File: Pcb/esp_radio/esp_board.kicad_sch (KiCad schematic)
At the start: 15 parts, among them J2 JTAG_ESP1, SW1 Reset, SW2 Boot, U3 ESP32-WROVER_IE

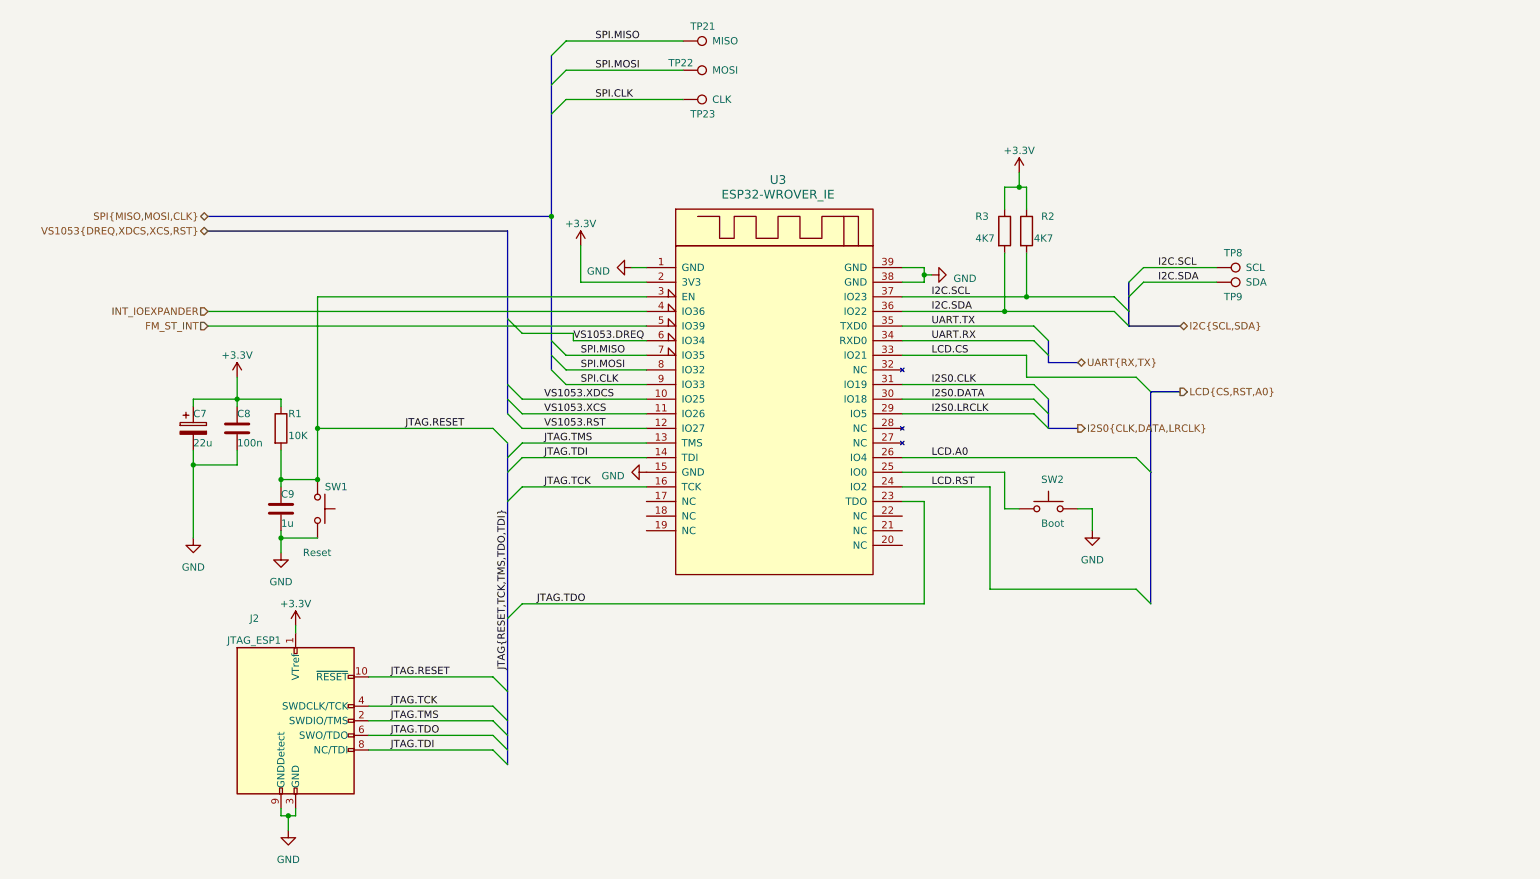
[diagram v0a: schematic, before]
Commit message: Move custom components to kicad_common_library.
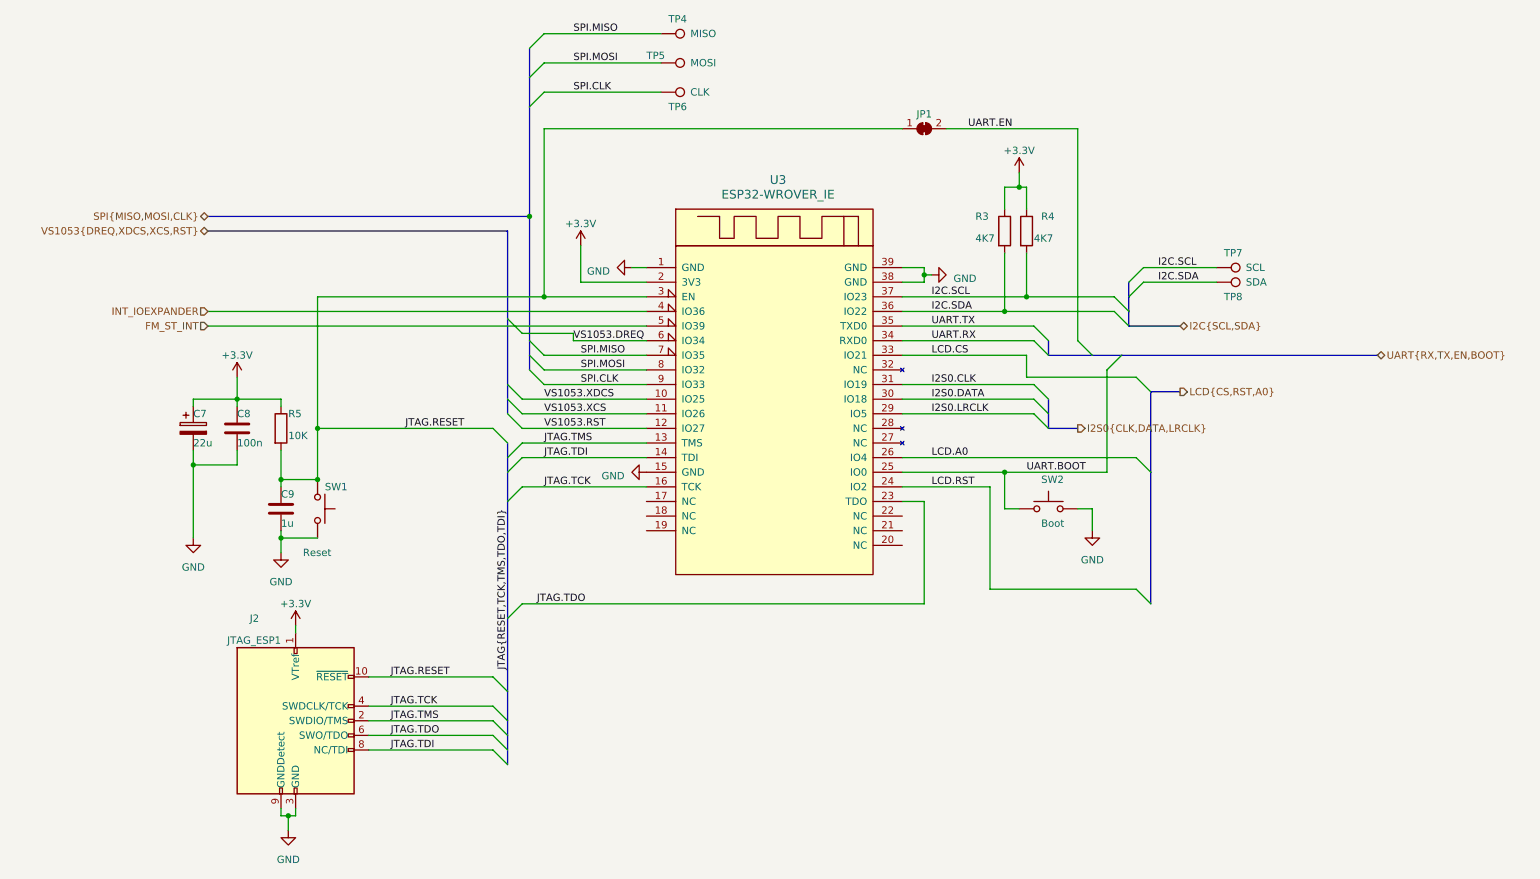
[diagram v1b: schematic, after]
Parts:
- added JP1: SolderJumper_2_Bridged, Jumper:SolderJumper-2_P1.3mm_Bridged_RoundedPad1.0x1.5mm, symbol Jumper:SolderJumper_2_Bridged
- U3: symbol KicadCommon:ESP32-WROVER -> kicad_common_lib:ESP32-WROVER
- renumbered R2 to R4, R1 to R5, TP21 to TP4, TP22 to TP5, TP23 to TP6, TP8 to TP7, TP9 to TP8
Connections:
- net JTAG.RESET: now also JP1.1 (A)
- net UART.BOOT: now reaches SW2.1, U3.25 (IO0)
- new net UART.EN: JP1.2 (B)
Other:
- moved on the sheet: TP4, TP5, TP6

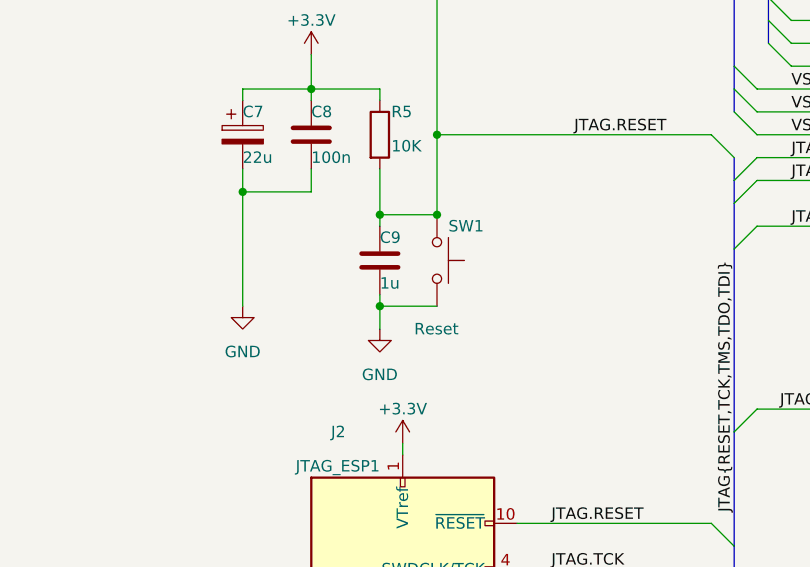
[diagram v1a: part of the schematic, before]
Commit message: Add components layout on PCB
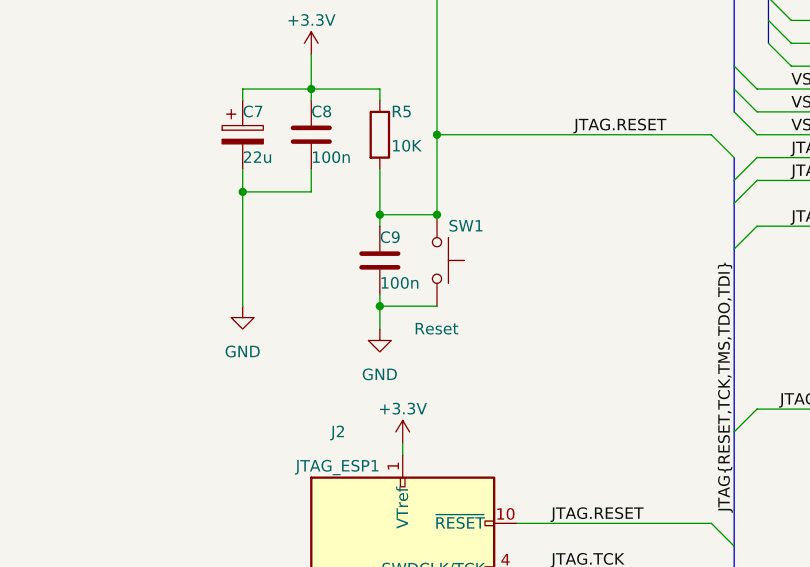
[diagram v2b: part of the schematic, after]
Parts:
- C9: value 1u -> 100n
- R3, R4: footprint Resistor_SMD:R_0805_2012Metric_Pad1.20x1.40mm_HandSolder -> kicad_common_lib:R_0805
- TP4, TP5, TP6, TP7, TP8: footprint (none) -> TestPoint:TestPoint_THTPad_D2.0mm_Drill1.0mm
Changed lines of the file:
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@@
       (effects (font (size 1.27 1.27)) (justify left))
     )
-    (property "Footprint" "" (at 128.27 46.99 0)
+    (property "Footprint" "TestPoint:TestPoint_THTPad_D2.0mm_Drill1.0mm" (at 128.27 46.99 0)
       (effects (font (size 1.27 1.27)) hide)
     )
@@
       (effects (font (size 1.27 1.27)) (justify left))
     )
-    (property "Footprint" "" (at 224.79 80.01 0)
+    (property "Footprint" "TestPoint:TestPoint_THTPad_D2.0mm_Drill1.0mm" (at 224.79 80.01 0)
       (effects (font (size 1.27 1.27)) hide)
     )
@@
       (effects (font (size 1.27 1.27)) (justify left))
     )
-    (property "Footprint" "" (at 224.79 77.47 0)
+    (property "Footprint" "TestPoint:TestPoint_THTPad_D2.0mm_Drill1.0mm" (at 224.79 77.47 0)
       (effects (font (size 1.27 1.27)) hide)
     )
@@
       (effects (font (size 1.27 1.27)) (justify left))
     )
-    (property "Value" "1u" (at 62.23 116.84 0)
+    (property "Value" "100n" (at 62.23 116.84 0)
       (effects (font (size 1.27 1.27)) (justify left))
     )
@@
       (effects (font (size 1.27 1.27)) (justify left))
     )
-    (property "Footprint" "Resistor_SMD:R_0805_2012Metric_Pad1.20x1.40mm_HandSolder" (at 189.992 66.04 90)
+    (property "Footprint" "kicad_common_lib:R_0805" (at 189.992 66.04 90)
       (effects (font (size 1.27 1.27)) hide)
     )
@@
       (effects (font (size 1.27 1.27)) (justify left))
     )
-    (property "Footprint" "" (at 128.27 41.91 0)
+    (property "Footprint" "TestPoint:TestPoint_THTPad_D2.0mm_Drill1.0mm" (at 128.27 41.91 0)
       (effects (font (size 1.27 1.27)) hide)
     )
@@
       (effects (font (size 1.27 1.27)) (justify left))
     )
-    (property "Footprint" "Resistor_SMD:R_0805_2012Metric_Pad1.20x1.40mm_HandSolder" (at 186.182 66.04 90)
+    (property "Footprint" "kicad_common_lib:R_0805" (at 186.182 66.04 90)
       (effects (font (size 1.27 1.27)) hide)
     )
@@
       (effects (font (size 1.27 1.27)) (justify left))
     )
-    (property "Footprint" "" (at 128.27 36.83 0)
-      (effects (font (size 1.27 1.27)) hide)
-    )
+    (property "Footprint" "TestPoint:TestPoint_THTPad_D2.0mm_Drill1.0mm" (at 128.27 36.83 0)
+      (effects (font (size 1.27 1.27)) hide)
+    )

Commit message: Finish board routing
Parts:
- added J11: IR, Connector_PinHeader_1.00mm:PinHeader_1x01_P1.00mm_Vertical, symbol Connector_Generic:Conn_01x01
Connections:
- net JTAG.TDO: now also J11.1 (Pin_1)
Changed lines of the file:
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@@
   (junction (at 46.99 106.68) (diameter 0.9144) (color 0 0 0 0)
   )
+  (junction (at 173.99 130.81) (diameter 0) (color 0 0 0 0)
+  )
   (junction (at 62.23 119.38) (diameter 0.9144) (color 0 0 0 0)
   )
@@
   (wire (pts (xy 77.47 143.51) (xy 99.06 143.51))
     (stroke (width 0) (type solid))
+  )
+  (wire (pts (xy 173.99 130.81) (xy 173.99 139.7))
+    (stroke (width 0) (type default))
   )
   (bus (pts (xy 105.41 39.37) (xy 105.41 44.45))
@@
         )
       )
+    )
+  )
+  (symbol (lib_id "Connector_Generic:Conn_01x01") (at 179.07 139.7 0) (unit 1)
+    (in_bom yes) (on_board yes) (dnp no) (fields_autoplaced)
+    (property "Reference" "J11" (at 181.61 139.065 0)
+      (effects (font (size 1.27 1.27)) (justify left))
+    )
+    (property "Value" "IR" (at 181.61 141.605 0)
+      (effects (font (size 1.27 1.27)) (justify left))
+    )
+    (property "Footprint" "Connector_PinHeader_1.00mm:PinHeader_1x01_P1.00mm_Vertical" (at 179.07 139.7 0)
+      (effects (font (size 1.27 1.27)) hide)
+    )
+    (property "Datasheet" "~" (at 179.07 139.7 0)
+      (effects (font (size 1.27 1.27)) hide)
+    )
+    (pin "1")
+    (instances
+      (project "esp_radio"
+        (path "/c9e2e0d2-0655-4f5e-8e13-71b41b1f7cfe/925b05c5-5253-4c9a-b090-487f8e9d1815"
+          (reference "J11") (unit 1)
+        )
+      )

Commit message: Add chip select emulation for i2c devices
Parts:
- J11: footprint Connector_PinHeader_1.00mm:PinHeader_1x01_P1.00mm_Vertical -> Connector_PinHeader_2.54mm:PinHeader_1x01_P2.54mm_Vertical
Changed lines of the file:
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@@
       (effects (font (size 1.27 1.27)) (justify left))
     )
-    (property "Footprint" "Connector_PinHeader_1.00mm:PinHeader_1x01_P1.00mm_Vertical" (at 179.07 139.7 0)
+    (property "Footprint" "Connector_PinHeader_2.54mm:PinHeader_1x01_P2.54mm_Vertical" (at 179.07 139.7 0)
       (effects (font (size 1.27 1.27)) hide)
     )

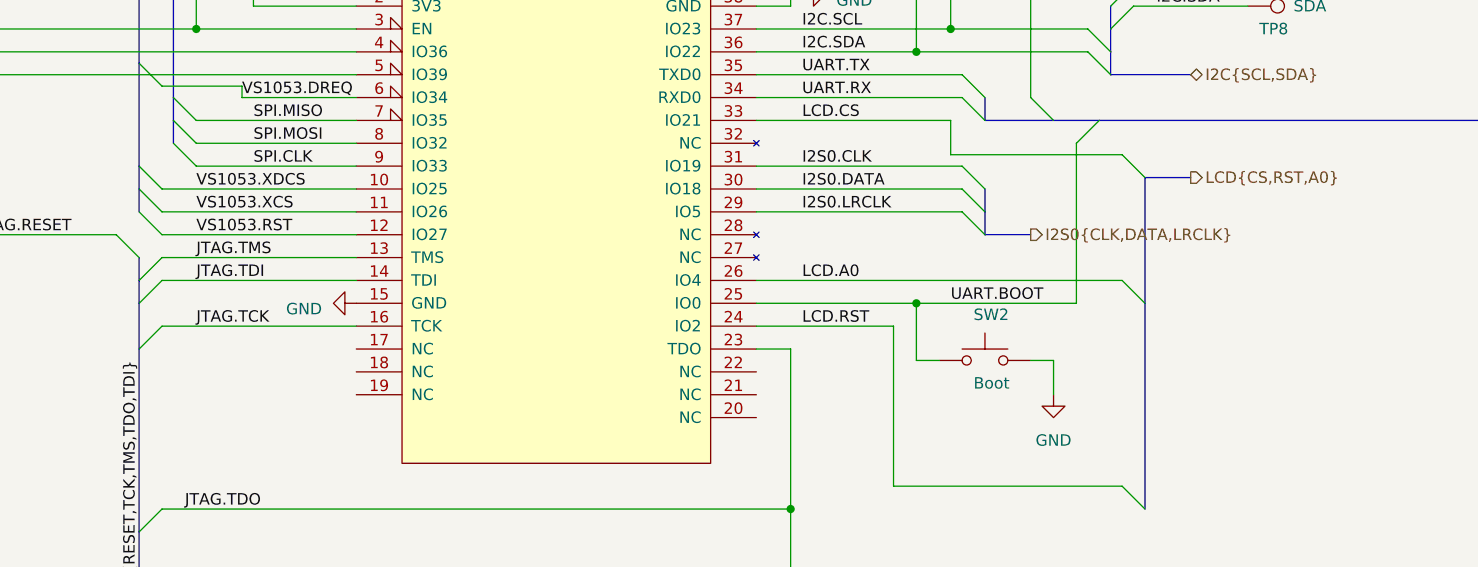
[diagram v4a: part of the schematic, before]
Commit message: Pcb. Fix hw issues.
Add loop to esp32 after i2s switcher
esp32 can convert stream to format compatible to MerusAudio.
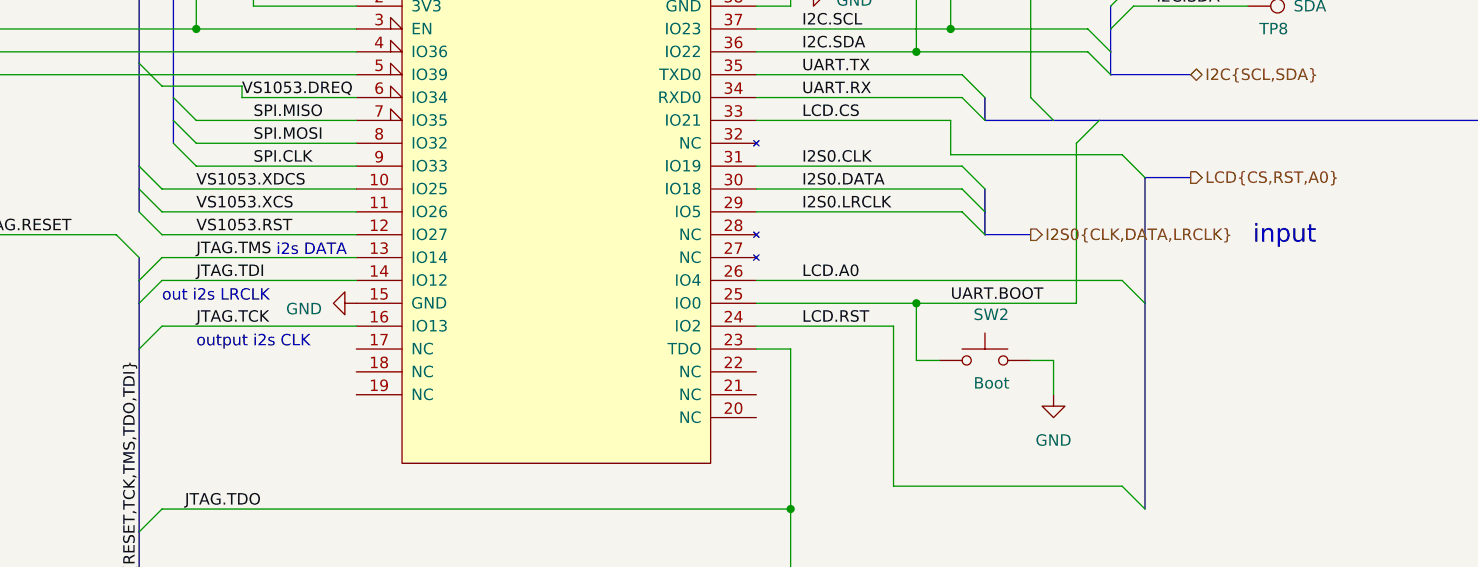
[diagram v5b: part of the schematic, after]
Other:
- note added: "i2s DATA"
- note added: "input"
- note added: "out i2s LRCLK"
- note added: "output i2s CLK"
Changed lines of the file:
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@@
     (stroke (width 0) (type default))
+  )
+  (text "output i2s CLK" (at 107.95 113.03 0)
+    (effects (font (size 1.27 1.27)) (justify left bottom))
+  )
+  (text "input" (at 232.41 101.6 0)
+    (effects (font (size 2 2)) (justify right bottom))
+  )
+  (text "out i2s LRCLK" (at 104.14 107.95 0)
+    (effects (font (size 1.27 1.27)) (justify left bottom))
+  )
+  (text "i2s DATA" (at 116.84 102.87 0)
+    (effects (font (size 1.27 1.27)) (justify left bottom))
   )
   (label "SPI.CLK" (at 114.3 92.71 0) (fields_autoplaced)
@@
     (pin "11")
     (pin "12")
-    (pin "13" (alternate "TMS"))
-    (pin "14" (alternate "TDI"))
+    (pin "13")
+    (pin "14")
     (pin "15")
-    (pin "16" (alternate "TCK"))
+    (pin "16")
     (pin "17" (alternate "NC"))
     (pin "18" (alternate "NC"))
